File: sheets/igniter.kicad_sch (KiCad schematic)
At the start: 18 parts, among them J2 Screw_Terminal_01x02, J4 Screw_Terminal_01x02, Q1 AO3400A, Q2 AO3400A

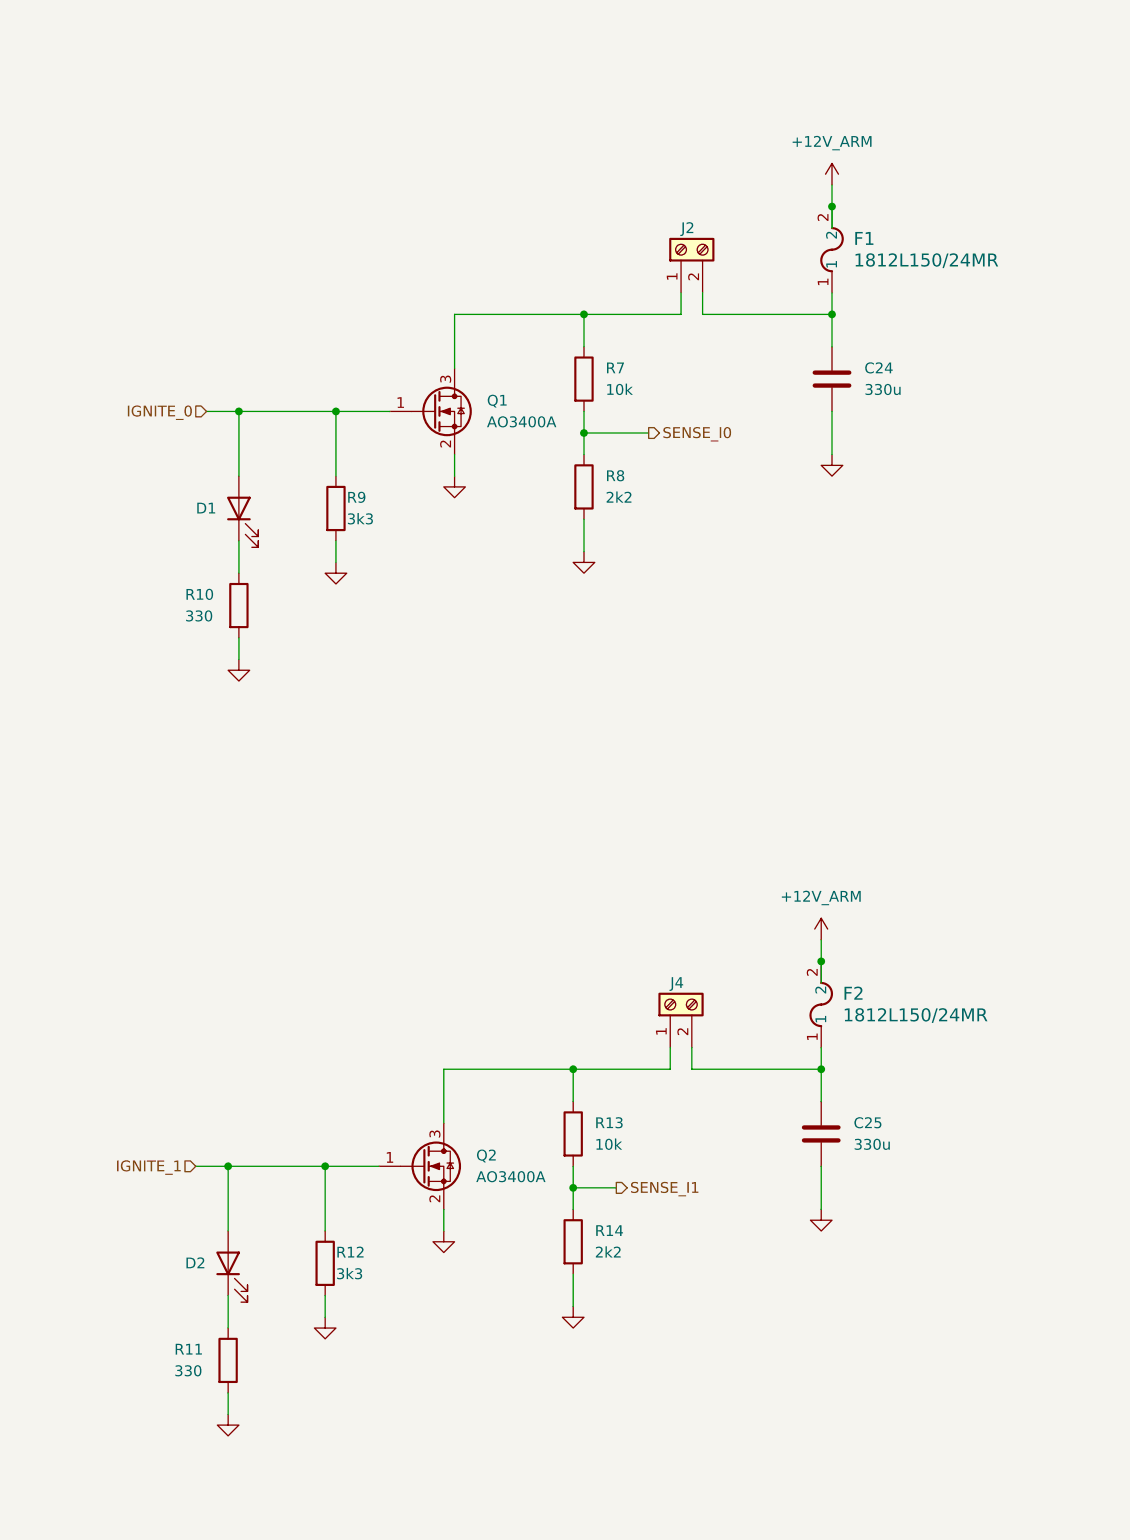
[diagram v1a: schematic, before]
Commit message: polished up circuit, added new 16.8V to 7.4V step down circuit components
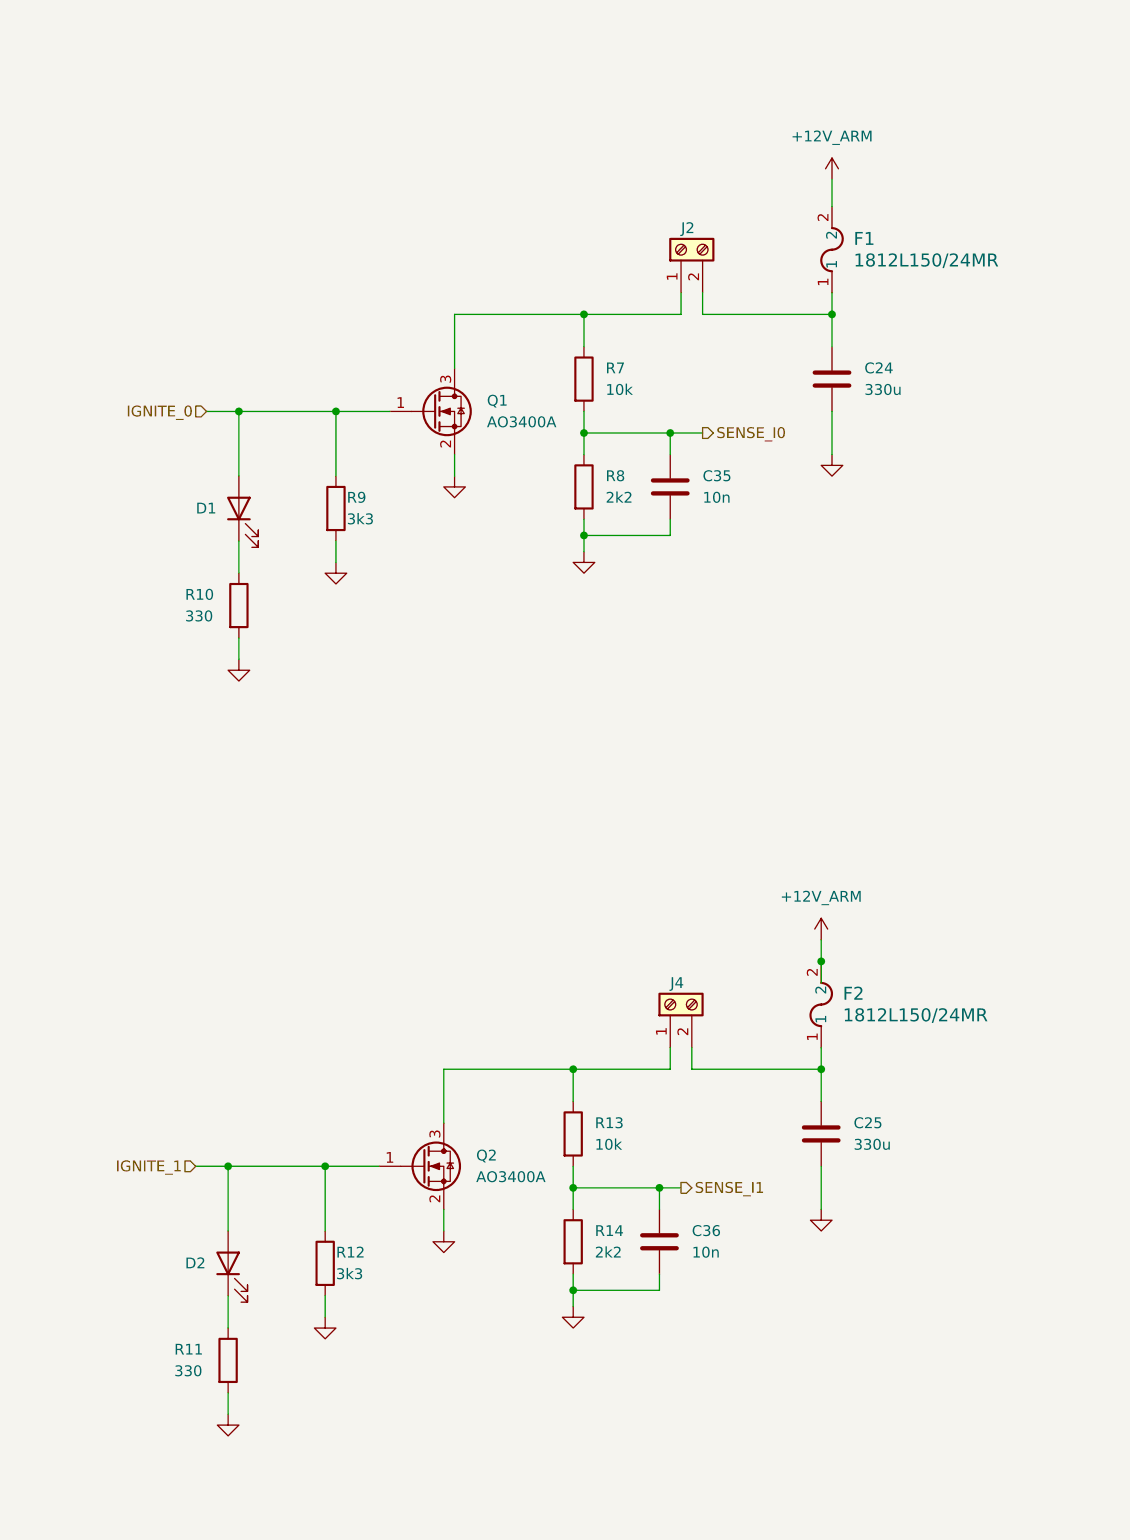
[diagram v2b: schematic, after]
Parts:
- added C35, C36: 10n, symbol Device:C
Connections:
- net GND: now also C35.2, C36.2
- net SENSE_I0: now also C35.1
- net SENSE_I1: now also C36.1

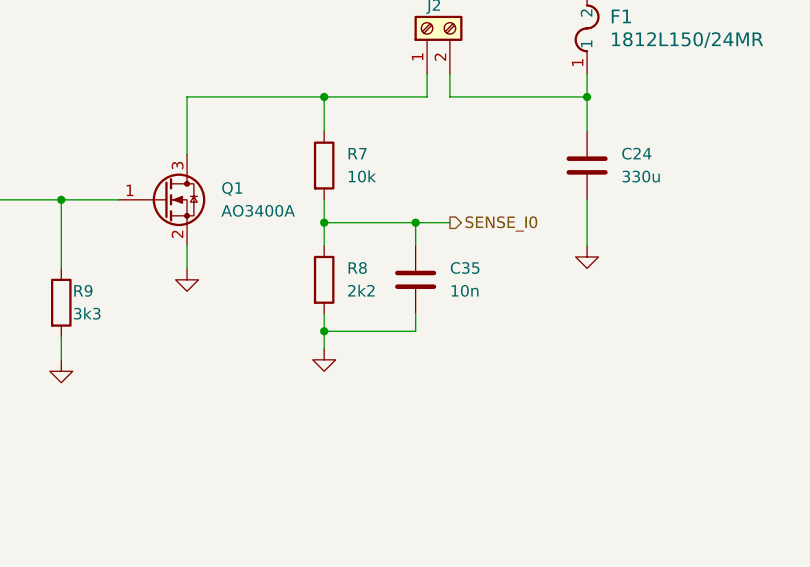
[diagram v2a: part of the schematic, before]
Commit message: added gpio connections in root, UART8, ADC2
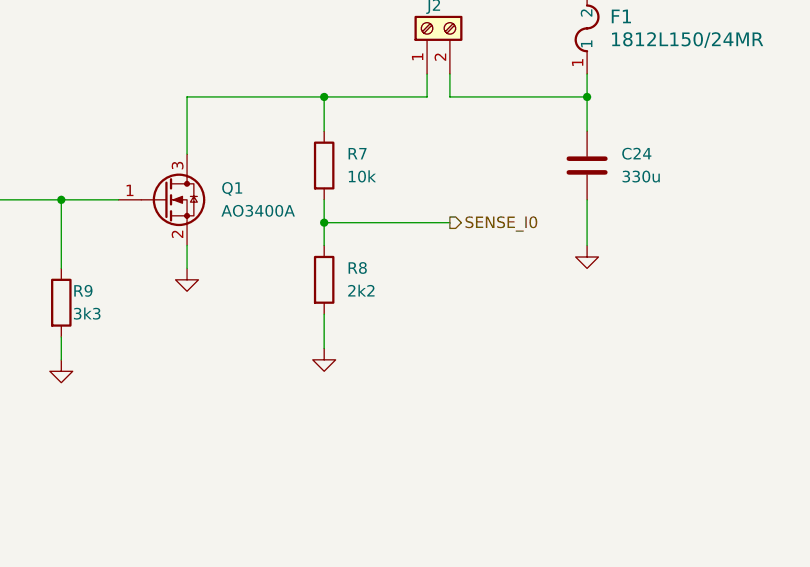
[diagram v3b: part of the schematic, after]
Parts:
- removed C35: 10n, symbol Device:C
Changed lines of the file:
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@@
-	)
-	(junction
-		(at 83.82 76.835)
-		(diameter 0)
-		(color 0 0 0 0)
 	)
 	(junction
@@
 	)
 	(junction
-		(at 93.98 64.77)
-		(diameter 0)
-		(color 0 0 0 0)
-	)
-	(junction
 		(at 82.55 165.735)
 		(diameter 0)
@@
 	(wire
 		(pts
-			(xy 83.82 74.93) (xy 83.82 76.835)
+			(xy 83.82 74.93) (xy 83.82 78.74)
 		)
 		(stroke
@@
 	(wire
 		(pts
-			(xy 83.82 64.77) (xy 93.98 64.77)
+			(xy 83.82 64.77) (xy 97.79 64.77)
 		)
 		(stroke
@@
 	(wire
 		(pts
-			(xy 93.98 74.93) (xy 93.98 76.835)
-		)
-		(stroke
-			(width 0)
-			(type default)
-		)
-	)
-	(wire
-		(pts
 			(xy 83.82 50.8) (xy 95.25 50.8)
 		)
@@
 	(wire
 		(pts
-			(xy 83.82 76.835) (xy 83.82 78.74)
-		)
-		(stroke
-			(width 0)
-			(type default)
-		)
-	)
-	(wire
-		(pts
 			(xy 82.55 153.67) (xy 82.55 156.21)
 		)
@@
 	(wire
 		(pts
-			(xy 93.98 64.77) (xy 97.79 64.77)
-		)
-		(stroke
-			(width 0)
-			(type default)
-		)
-	)
-	(wire
-		(pts
 			(xy 54.61 77.47) (xy 54.61 80.01)
 		)
@@
 	(wire
 		(pts
-			(xy 93.98 64.77) (xy 93.98 67.31)
-		)
-		(stroke
-			(width 0)
-			(type default)
-		)
-	)
-	(wire
-		(pts
 			(xy 68.58 67.31) (xy 68.58 69.85)
 		)
@@
 		(pts
 			(xy 54.61 62.23) (xy 54.61 69.85)
-		)
-		(stroke
-			(width 0)
-			(type default)
-		)
-	)
-	(wire
-		(pts
-			(xy 93.98 76.835) (xy 83.82 76.835)
 		)
 		(stroke
@@
 					(unit 1)
 				)
-			)
-		)
-	)
-	(symbol
-		(lib_id "Device:C")
-		(at 93.98 71.12 0)
-		(unit 1)
-		(exclude_from_sim no)
-		(in_bom yes)
-		(on_board yes)
-		(dnp no)
-		(fields_autoplaced yes)
-		(property "Reference" "C35"
-			(at 97.79 69.8499 0)
-			(effects
-				(font
-					(size 1.27 1.27)
-				)
-				(justify left)
-			)
-		)
-		(property "Value" "10n"
-			(at 97.79 72.3899 0)
-			(effects
-				(font
-					(size 1.27 1.27)
-				)
-				(justify left)
-			)
-		)
-		(property "Footprint" ""
-			(at 94.9452 74.93 0)
-			(effects
-				(font
-					(size 1.27 1.27)
-				)
-				(hide yes)
-			)
-		)
-		(property "Datasheet" "~"
-			(at 93.98 71.12 0)
-			(effects
-				(font
-					(size 1.27 1.27)
-				)
-				(hide yes)
-			)
-		)
-		(property "Description" "Unpolarized capacitor"
-			(at 93.98 71.12 0)
-			(effects
-				(font
-					(size 1.27 1.27)
-				)
-				(hide yes)
-			)
-		)
-		(pin "1"
-		)
-		(pin "2"
-		)
-		(instances
-			(project ""
-				(path "/3f5bc5ea-feaa-4ed9-b0e0-c918b1fb5754/52f7934e-6b3c-4046-8930-cc057f9c6816"
-					(reference "C35")
-					(unit 1)
-				)

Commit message: final rev1
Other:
- note added: "Drogue"
- note added: "Main"
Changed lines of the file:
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@@
 	(generator_version "9.0")
 	(paper "A4")
+	(rectangle
+		(start 17.145 15.875)
+		(end 145.415 101.6)
+		(stroke
+			(width 0.2032)
+			(type solid)
+		)
+		(fill
+			(type none)
+		)
+	)
+	(rectangle
+		(start 17.78 107.315)
+		(end 146.05 193.04)
+		(stroke
+			(width 0.2032)
+			(type solid)
+		)
+		(fill
+			(type none)
+		)
+	)
+	(text "Drogue"
+		(exclude_from_sim no)
+		(at 136.525 98.425 0)
+		(effects
+			(font
+				(size 2.54 2.54)
+				(thickness 0.508)
+				(bold yes)
+			)
+		)
+	)
+	(text "Main"
+		(exclude_from_sim no)
+		(at 137.16 187.96 0)
+		(effects
+			(font
+				(size 2.54 2.54)
+				(thickness 0.508)
+				(bold yes)
+			)
+		)
+	)
 	(junction
 		(at 113.03 50.8)

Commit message: Rev1 schematic done
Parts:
- removed C36: 10n, symbol Device:C
- renumbered C25 to C46, C24 to C47, D2 to D7, D1 to D8, F2 to F3, F1 to F4, J4 to J18, J2 to J19, Q1 to Q3, R11 to R39, R10 to R40, R12 to R41, R9 to R42, R13 to R43, R14 to R44, R7 to R45, R8 to R46

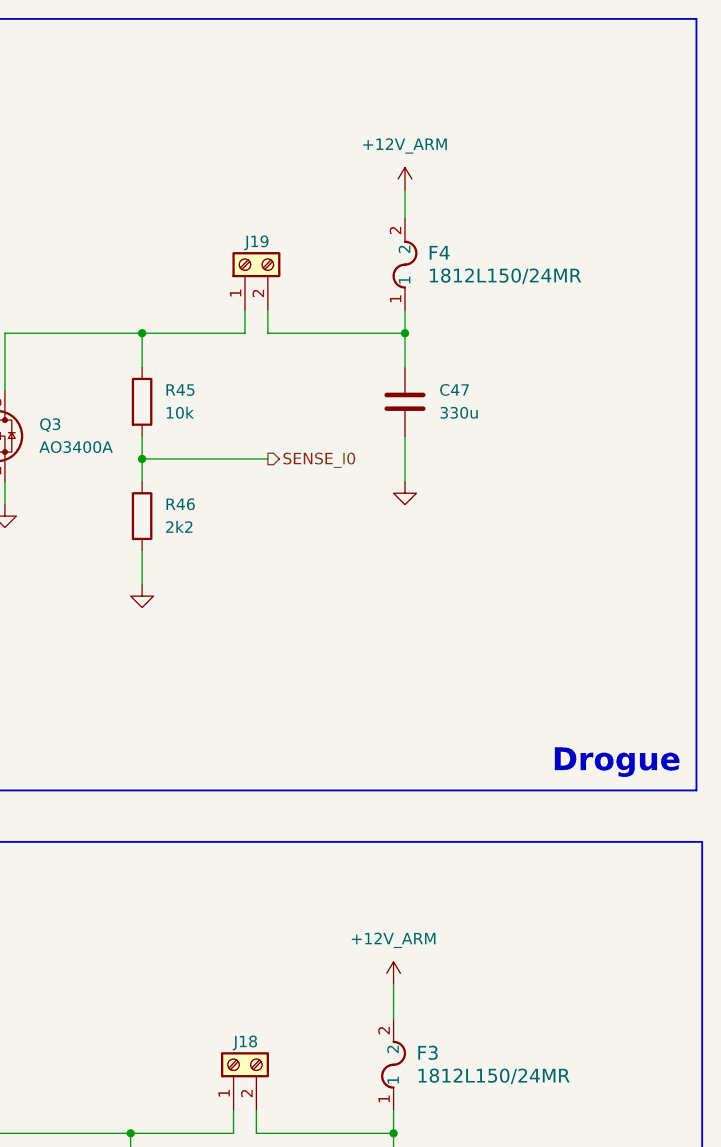
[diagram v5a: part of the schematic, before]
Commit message: Cleared ALL ERC warnings
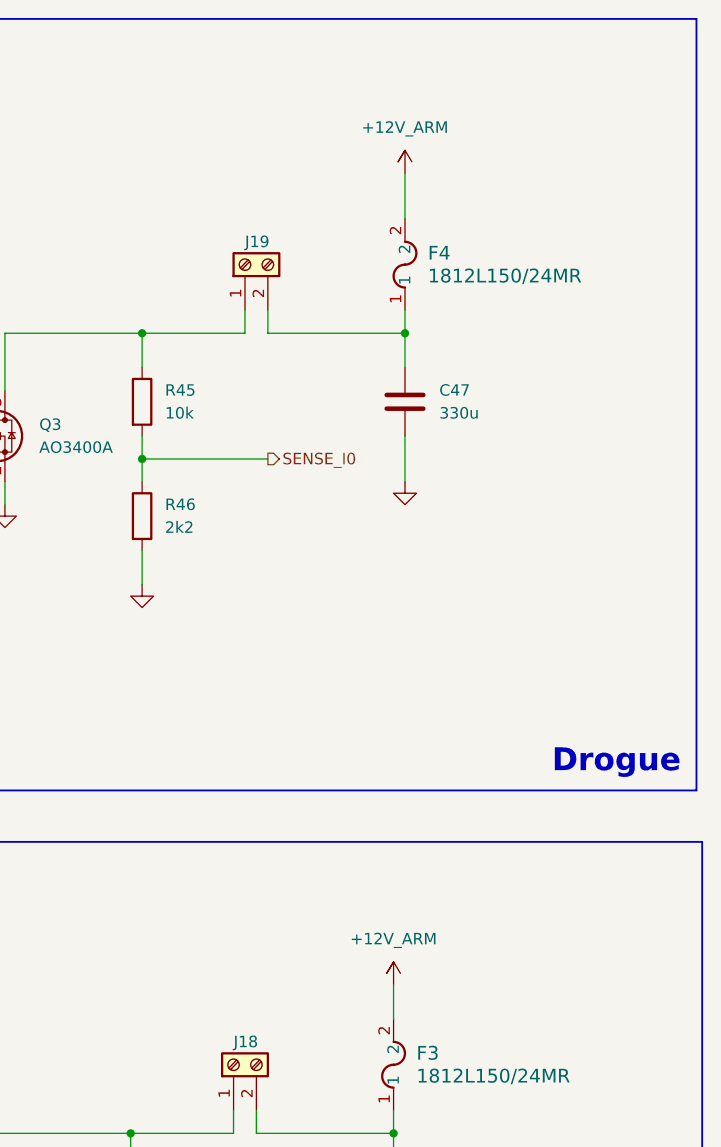
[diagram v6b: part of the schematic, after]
